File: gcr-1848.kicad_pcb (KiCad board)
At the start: 2 copper layers, 71.1 x 12.7 mm, 28 parts

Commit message: Updated gerbers and board design
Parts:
- moved R1 113.1 mm to (130.2, 106.7)
- moved R2 113.1 mm to (122.6, 106.7)
- moved ? 113.1 mm to (106.7, 101.6)
- moved ? 113.1 mm to (106.0, 97.2)
- moved ? 113.1 mm to (106.0, 106.0)
- moved ? 113.1 mm to (116.2, 106.0)
- moved ? 113.1 mm to (116.2, 97.2)
- moved ? 113.1 mm to (152.4, 106.0)
- moved ? 113.1 mm to (149.9, 104.1)
- moved ? 113.1 mm to (128.9, 101.6)
- moved ? 113.1 mm to (163.8, 101.6)
- moved C2 113.1 mm to (128.9, 101.6)
- moved C3 113.1 mm to (121.3, 101.6)
- moved D1 113.1 mm to (134.6, 101.9)
- moved R3 113.1 mm to (154.3, 100.3)
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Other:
- board size 71.1 x 12.7 mm -> 76.2 x 12.7 mm

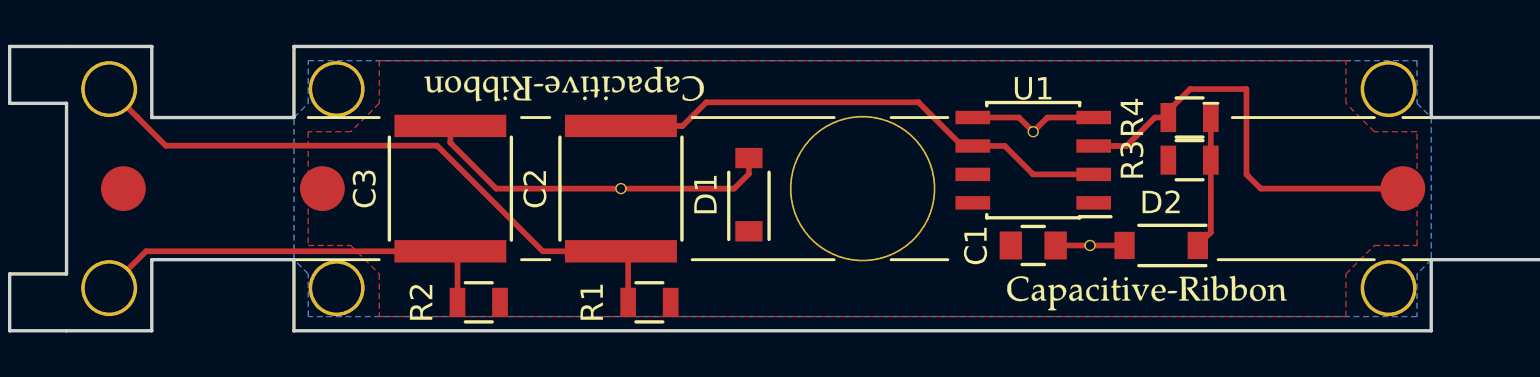
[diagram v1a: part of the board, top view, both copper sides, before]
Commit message: Updated PCB and rearranged schematic
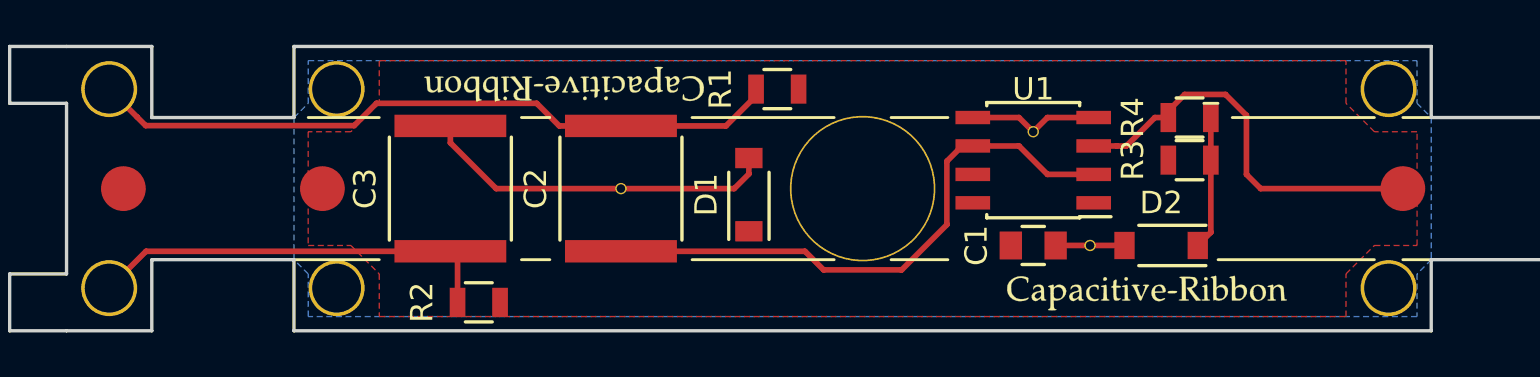
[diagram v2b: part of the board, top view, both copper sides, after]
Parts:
- D1: value (none) -> 24V
- R1: value 6.8k -> (none)
- moved R1 11.1 mm to (135.9, 97.2)
- turned C1 to 180 degrees
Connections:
- ? pad 1: Net-(C2-Pad2) -> Net-(C2-Pad1)
- C1 pad 1: +24V -> Earth
- C1 pad 2: Earth -> +24V
- R1 pad 2: Net-(C2-Pad2) -> Net-(C2-Pad1)
- U1 pad 2: Net-(C2-Pad1) -> Net-(C2-Pad2)
- U1 pad 6: Net-(C2-Pad1) -> Net-(C2-Pad2)
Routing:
- net Net-(C2-Pad1): track 23.4 -> 31.3 mm
- net Net-(C2-Pad2): track 28.3 -> 26.9 mm
- net Net-(C4-Pad2): track 19.6 -> 18.7 mm
